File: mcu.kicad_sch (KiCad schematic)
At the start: 65 parts, among them J10 Micro_SD_Card, J11 Conn_01x06, J12 Conn_01x02, J13 USB_B, J14 USB_B, J15 Conn_01x01, J16 Conn_01x01, J8 Conn_02x05_Odd_Even, J9 Conn_01x06, SW1 SW_Push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

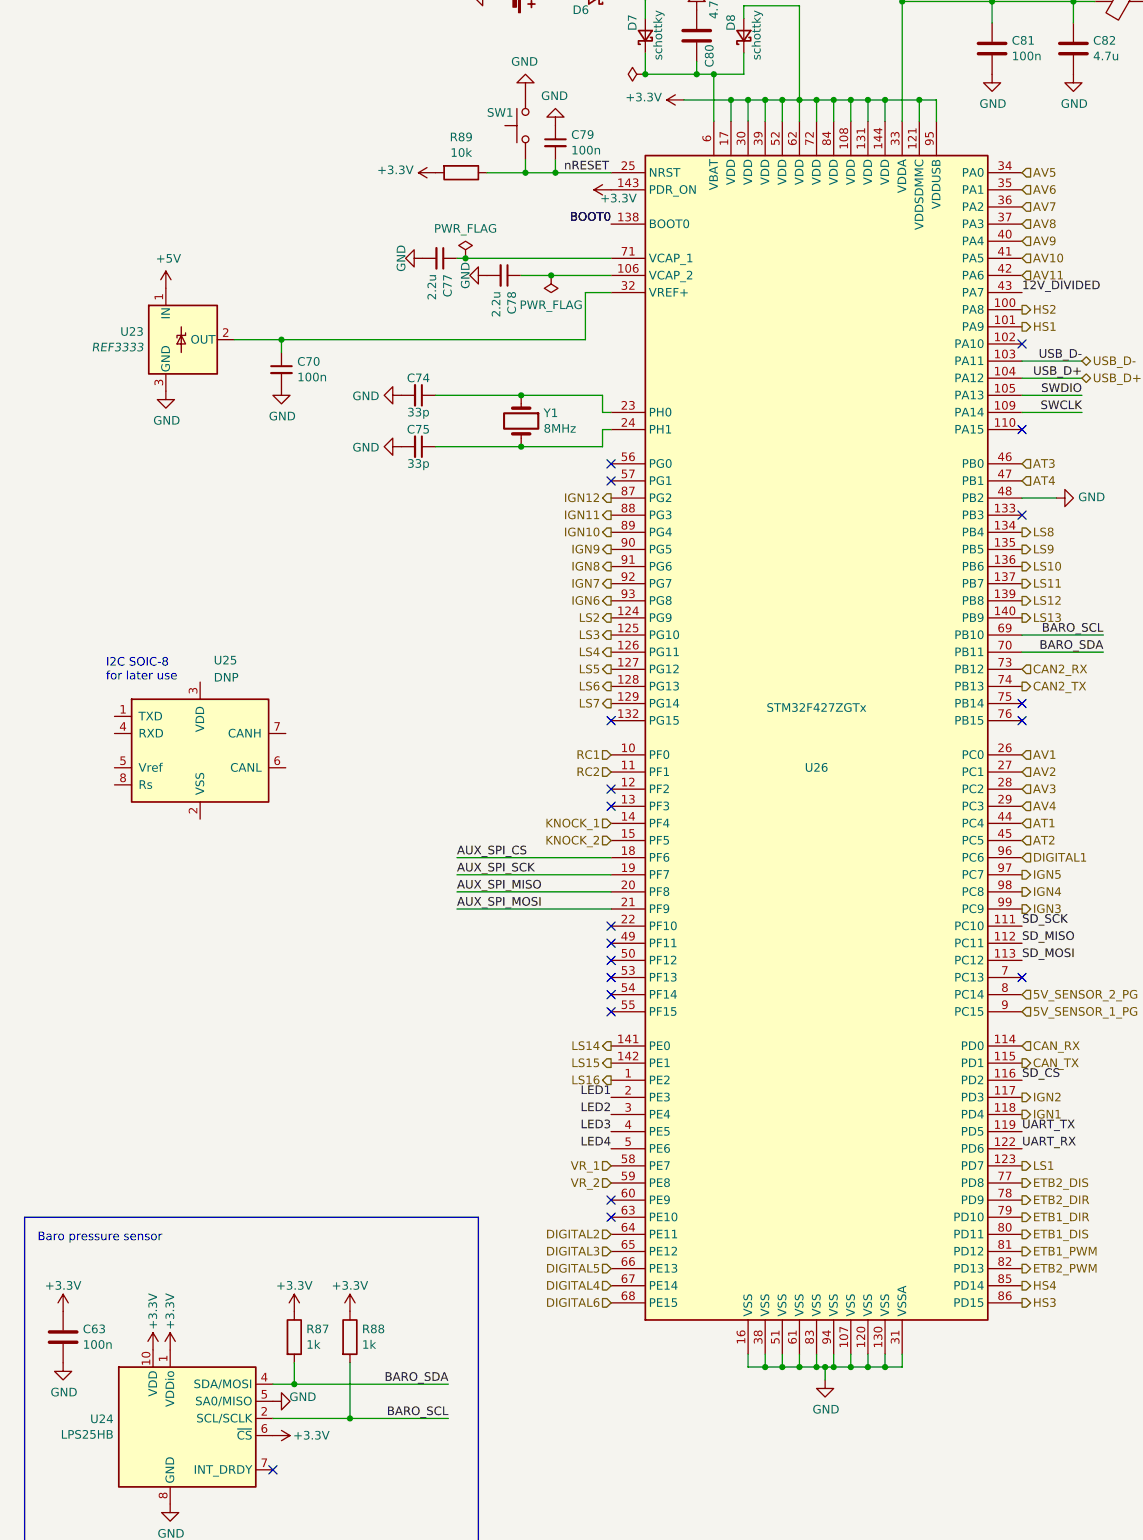
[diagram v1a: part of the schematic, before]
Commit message: make hardware updates: - fix erc/drc errors - switch to VNLD5090 - switch to SOIC8 ignition drivers - BOM deduplication of similar parts
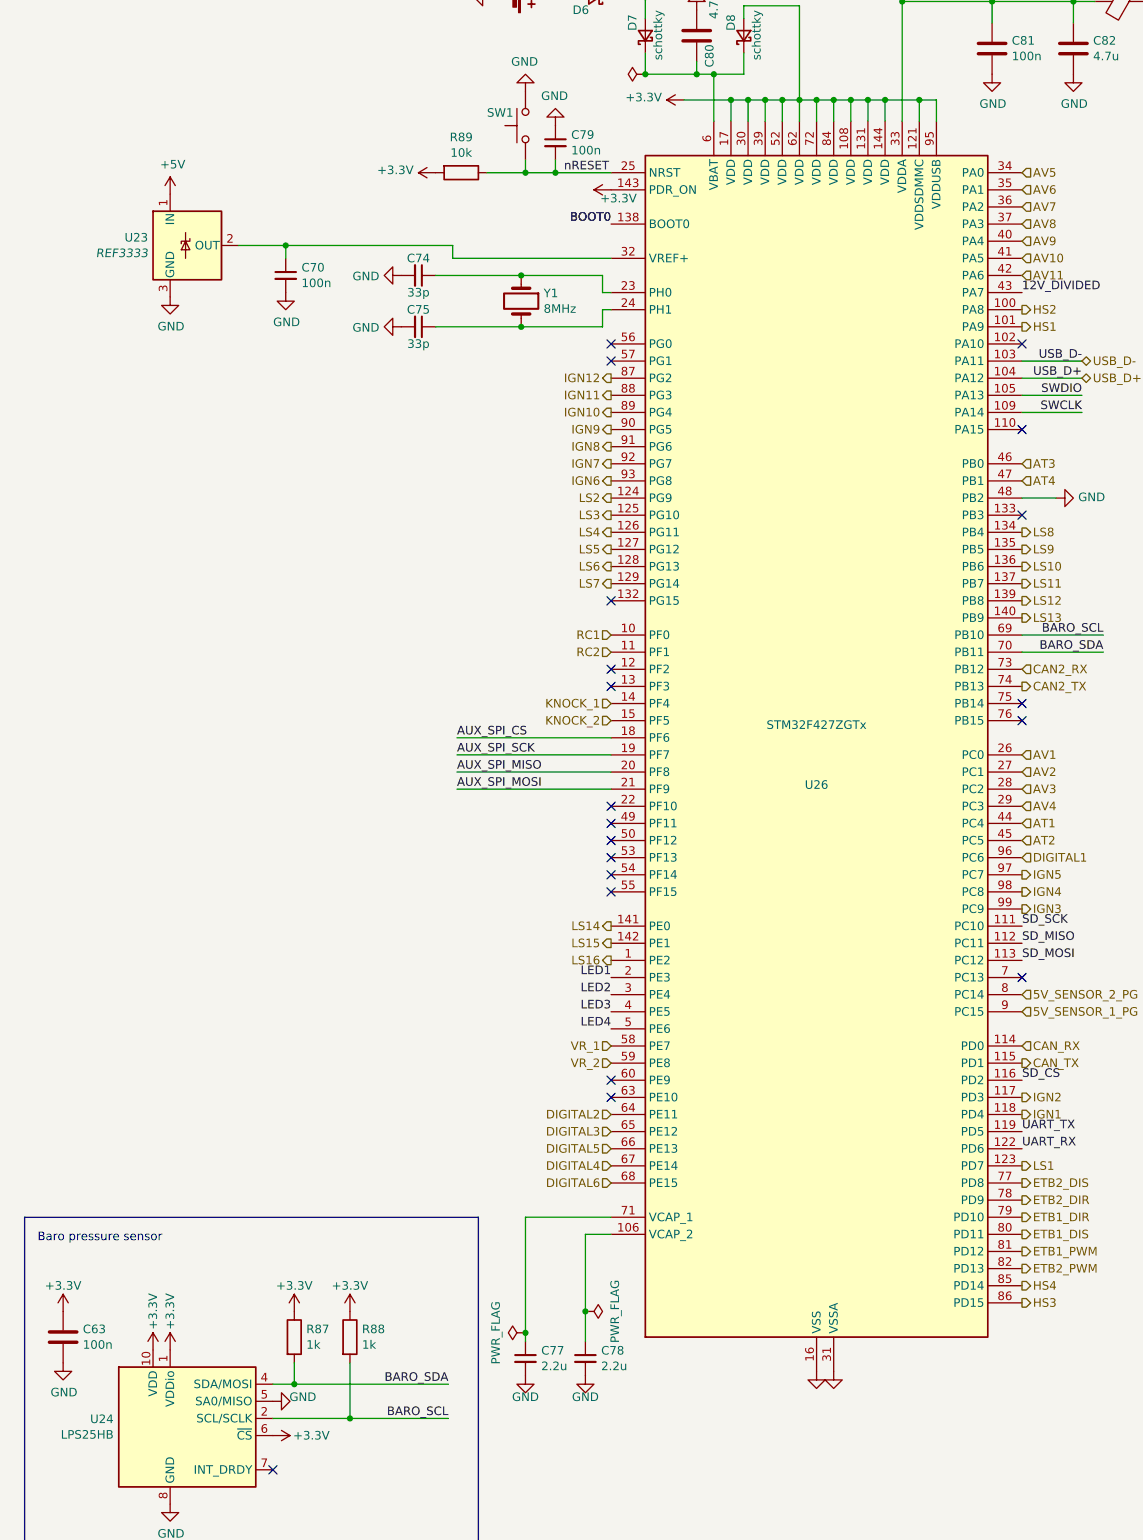
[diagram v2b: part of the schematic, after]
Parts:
- removed U25: DNP, Package_SO:SOIC-8_3.9x4.9mm_P1.27mm, symbol Interface_CAN_LIN:MCP2551-I-SN
- U26: LCSC C117816 -> C90235
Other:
- note removed: "I2C SOIC-8 for later use"
- moved on the sheet: C70, C74, C75, C77, C78, U23, Y1

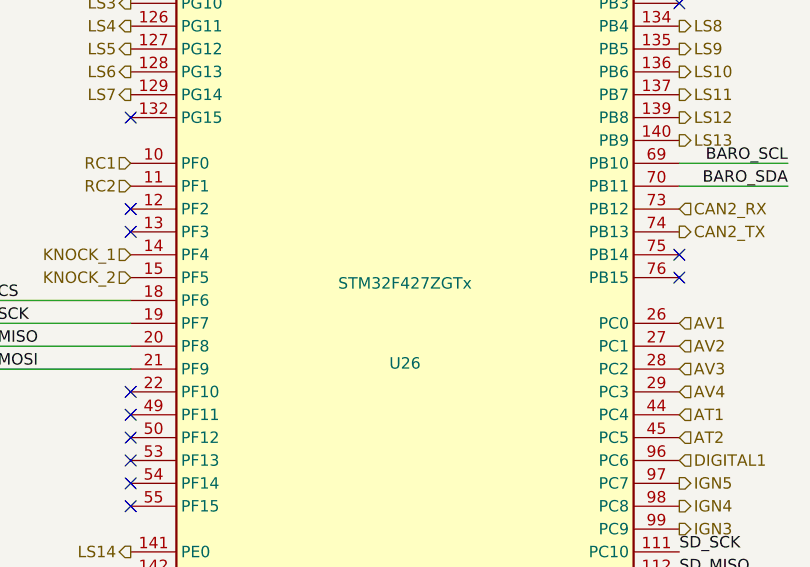
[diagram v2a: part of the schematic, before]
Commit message: correct MCU PN
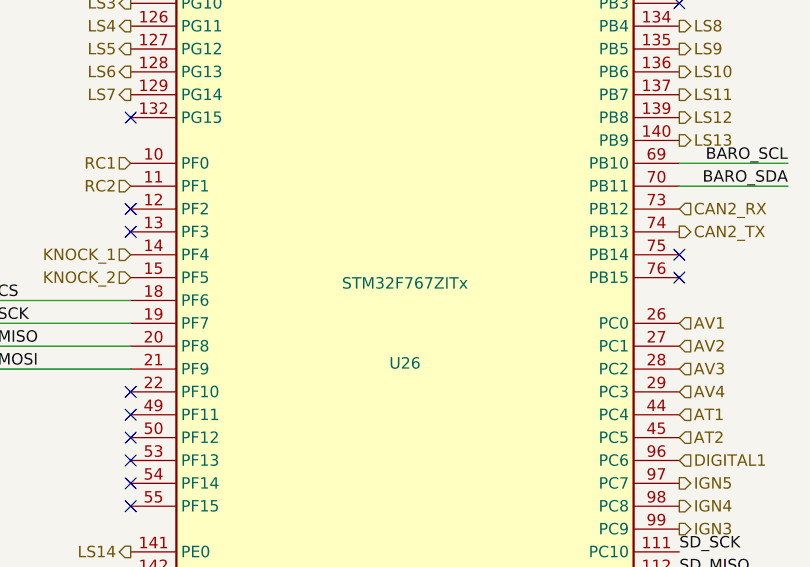
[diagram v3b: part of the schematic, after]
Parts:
- U26: value STM32F427ZGTx -> STM32F767ZITx
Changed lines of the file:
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@@
       (effects (font (size 1.27 1.27)))
     )
-    (property "Value" "STM32F427ZGTx" (at 134.62 157.48 0)
+    (property "Value" "STM32F767ZITx" (at 134.62 157.48 0)
       (effects (font (size 1.27 1.27)))
     )

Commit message: 1.6 BOM tweaks, outputs draft
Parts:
- U27: LCSC C7519 -> C111212
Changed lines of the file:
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@@
       (effects (font (size 1.27 1.27)) hide)
     )
-    (property "LCSC" "C7519" (at 281.94 111.125 0)
+    (property "LCSC" "C111212" (at 281.94 111.125 0)
       (effects (font (size 1.27 1.27)) hide)
     )

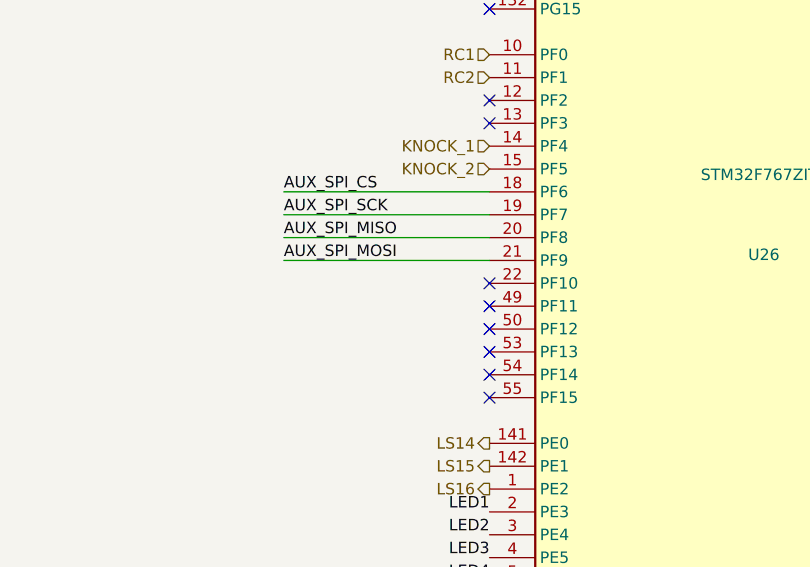
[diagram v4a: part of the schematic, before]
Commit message: route trigger scope
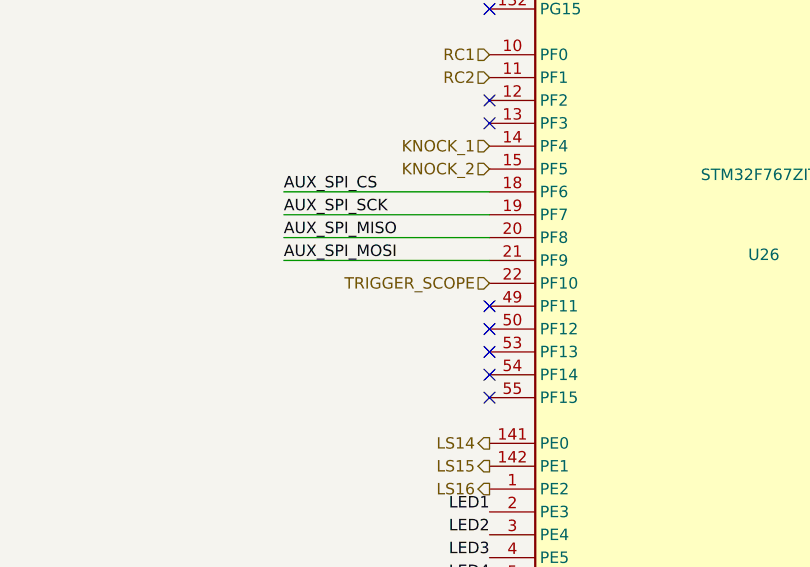
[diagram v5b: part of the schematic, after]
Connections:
- net TRIGGER_SCOPE: now reaches U26.22 (PF10)
- no-connect marks 29 -> 28
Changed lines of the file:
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@@
   (no_connect (at 104.14 212.725))
   (no_connect (at 336.55 44.45))
-  (no_connect (at 104.14 169.545))
   (no_connect (at 53.975 267.97))
   (no_connect (at 104.14 149.225))
@@
     (effects (font (size 1.27 1.27)) (justify right))
   )
+  (hierarchical_label "TRIGGER_SCOPE" (shape input) (at 104.14 169.545 180) (fields_autoplaced)
+    (effects (font (size 1.27 1.27)) (justify right))
+  )
